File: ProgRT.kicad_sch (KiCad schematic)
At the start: 66 parts

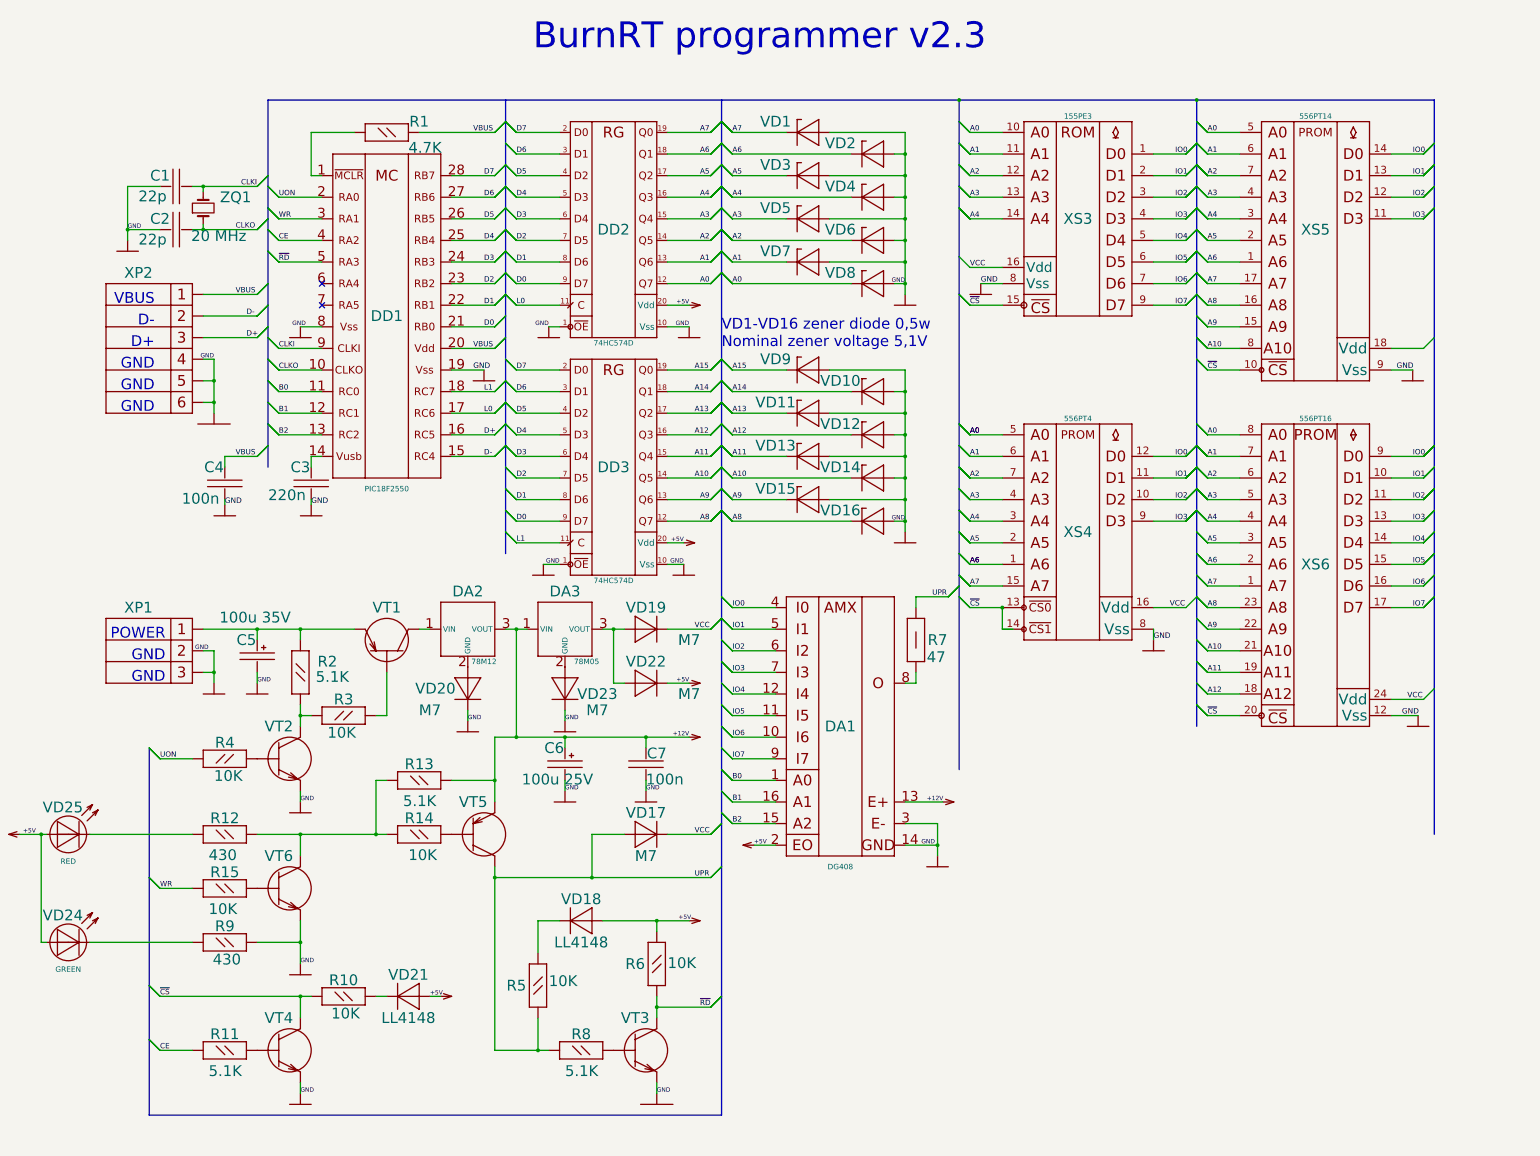
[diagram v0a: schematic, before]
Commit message: PCB from the original single-board layout
Recovered the PCB from schematic and old gerbers. The gerbers didn't contain
recent fixups, these parts need to be placed
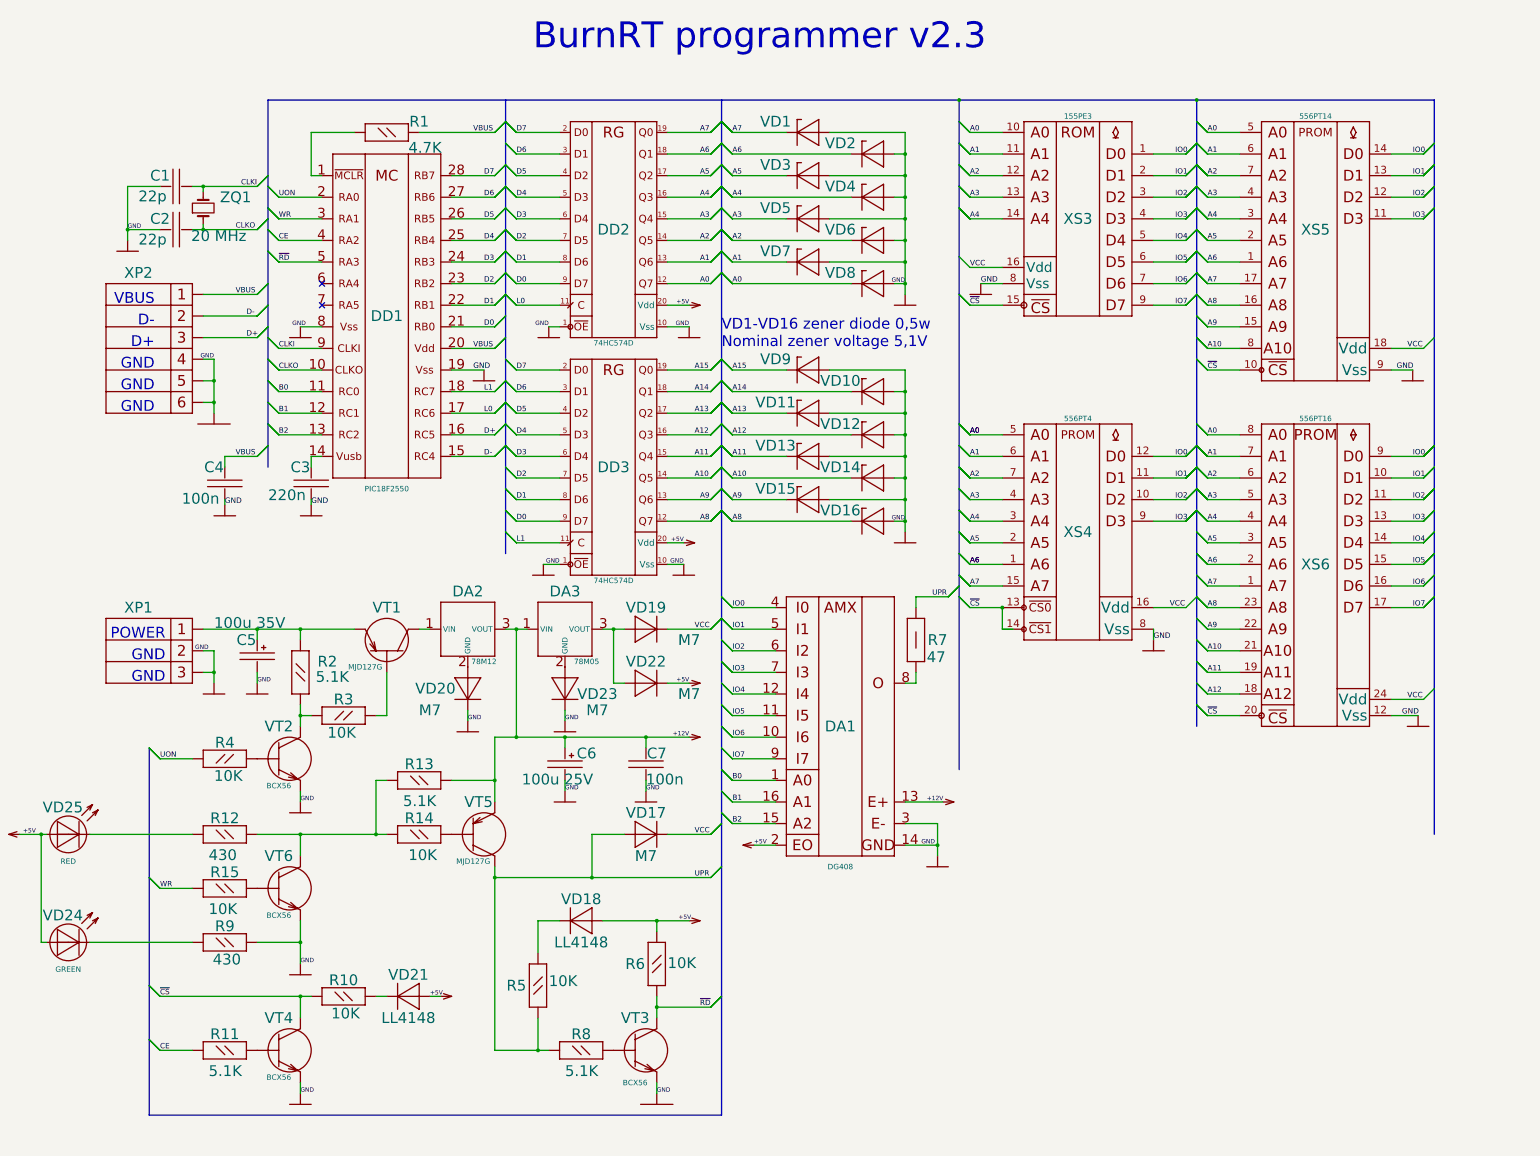
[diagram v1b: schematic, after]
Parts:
- C1, C2: footprint ProgRT: -> Capacitor_SMD:C_0805_2012Metric_Pad1.18x1.45mm_HandSolder
- C3, C4, C7: footprint (none) -> Capacitor_SMD:C_0805_2012Metric_Pad1.18x1.45mm_HandSolder
- C5, C6: footprint (none) -> Capacitor_THT:CP_Radial_D5.0mm_P2.50mm
- VD24, VD25: footprint Socet.SCH.eagle: -> Diode_SMD:D_SOD-123
- VT1, VT5: value КТ973 -> MJD127G; footprint (none) -> Package_TO_SOT_SMD:TO-252-2
- VT2, VT3, VT4, VT6: value КТ503 -> BCX56; footprint (none) -> Package_TO_SOT_SMD:SOT-89-3
- XP2: footprint Connector_USB:USB_Micro-B_Wuerth_629105150521 -> Connector_USB:USB_Mini-B_Lumberg_2486_01_Horizontal
- XS6: footprint Socket:DIP_Socket-24_W4.3_W5.08_W7.62_W10.16_W10.9_3M_224-5248-00-0602J -> Socket:DIP_Socket-24_W11.9_W12.7_W15.24_W17.78_W18.5_3M_224-1275-00-0602J
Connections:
- net +12V: now also C6.1, VT5.3 (E); no longer C6.2 (1), VT5.2 (E)
- net GND: now also C5.2, C6.2; no longer C5.1 (2), C6.1 (2)
- net UPR: now also VT5.2 (C); no longer VT5.1 (C)
- net VCC: now also XS5.18 (Vdd)
- net at R14.2: now also VT5.1 (B); no longer VT5.3 (B)
- net at DA2.1 (VIN): now also VT1.2 (C); no longer VT1.1 (C)
- net at R2.2, XP1.1: now also C5.1, VT1.3 (E); no longer C5.2 (1), VT1.2 (E)
- net at R3.2: now also VT1.1 (B); no longer VT1.3 (B)

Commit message: Add missing parts
ICSP connector and C8 capacitor
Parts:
- added C8: 100n, Capacitor_SMD:C_0805_2012Metric_Pad1.18x1.45mm_HandSolder, symbol ProgRT-eagle-import:K10-17_1
- added XP3: Conn_01x06, Connector_PinHeader_2.54mm:PinHeader_1x06_P2.54mm_Vertical, symbol Connector_Generic:Conn_01x06
- VD24, VD25: footprint Diode_SMD:D_SOD-123 -> Diode_SMD:D_SOD-123F
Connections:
- net +5V: now also C8.2 (1)
- net D5: now also XP3.6 (Pin_6)
- net D6: now also XP3.5 (Pin_5)
- net D7: now also XP3.4 (Pin_4)
- net GND: now also C8.1 (2), XP3.3 (Pin_3)
- net VBUS: now also XP3.2 (Pin_2)
- net MCLR: now reaches DD1.1 (!MCLR), R1.1
- net MCLR: now also XP3.1 (Pin_1)

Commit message: Small footprint corrections
- use SMF footprint for Zener diodes, easier to hand-solder
- use larger footprint for polar caps, extends availability
- use 3216 LEDs, easier available and easier to hand-solder
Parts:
- C5, C6: footprint Capacitor_THT:CP_Radial_D5.0mm_P2.50mm -> Capacitor_THT:CP_Radial_D8.0mm_P3.80mm
- C8: footprint Capacitor_SMD:C_0805_2012Metric_Pad1.18x1.45mm_HandSolder -> Capacitor_SMD:C_1206_3216Metric_Pad1.33x1.80mm_HandSolder
- VD1, VD10, VD11, VD12, VD13, VD14, VD15, VD16, VD2, VD3, VD4, VD5, VD6, VD7, VD8, VD9: footprint Diode_SMD:D_SOD-123 -> Diode_SMD:D_SMF
- VD24, VD25: footprint Diode_SMD:D_SOD-123F -> LED_SMD:LED_1206_3216Metric_Pad1.42x1.75mm_HandSolder
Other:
- note removed: "BurnRT programmer v2.3"
- title: (none) -> BurnRT programmer
- moved on the sheet: C1, C2, C3, C4, C5, C6, C7, C8, DA1, DA2, DA3, DD1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

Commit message: Use MiniMELF Zeners
Change Zener diodes package again to MiniMELF. Should be easier to hand-solder.
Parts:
- VD1, VD10, VD11, VD12, VD13, VD14, VD15, VD16, VD2, VD3, VD4, VD5, VD6, VD7, VD8, VD9: footprint Diode_SMD:D_SMF -> Diode_SMD:D_MiniMELF
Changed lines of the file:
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@@
       (effects (font (size 1.27 1.27)) hide)
     )
-    (property "Footprint" "Diode_SMD:D_SMF" (id 2) (at 220.98 66.04 0)
+    (property "Footprint" "Diode_SMD:D_MiniMELF" (id 2) (at 220.98 66.04 0)
       (effects (font (size 1.27 1.27)) hide)
     )
@@
       (effects (font (size 1.27 1.27)) hide)
     )
-    (property "Footprint" "Diode_SMD:D_SMF" (id 2) (at 236.22 50.8 0)
+    (property "Footprint" "Diode_SMD:D_MiniMELF" (id 2) (at 236.22 50.8 0)
       (effects (font (size 1.27 1.27)) hide)
     )
@@
       (effects (font (size 1.27 1.27)) hide)
     )
-    (property "Footprint" "Diode_SMD:D_SMF" (id 2) (at 236.22 106.68 0)
+    (property "Footprint" "Diode_SMD:D_MiniMELF" (id 2) (at 236.22 106.68 0)
       (effects (font (size 1.27 1.27)) hide)
     )
@@
       (effects (font (size 1.27 1.27)) hide)
     )
-    (property "Footprint" "Diode_SMD:D_SMF" (id 2) (at 236.22 127 0)
+    (property "Footprint" "Diode_SMD:D_MiniMELF" (id 2) (at 236.22 127 0)
       (effects (font (size 1.27 1.27)) hide)
     )
@@
       (effects (font (size 1.27 1.27)) hide)
     )
-    (property "Footprint" "Diode_SMD:D_SMF" (id 2) (at 220.98 76.2 0)
+    (property "Footprint" "Diode_SMD:D_MiniMELF" (id 2) (at 220.98 76.2 0)
       (effects (font (size 1.27 1.27)) hide)
     )
@@
       (effects (font (size 1.27 1.27)) hide)
     )
-    (property "Footprint" "Diode_SMD:D_SMF" (id 2) (at 220.98 121.92 0)
+    (property "Footprint" "Diode_SMD:D_MiniMELF" (id 2) (at 220.98 121.92 0)
       (effects (font (size 1.27 1.27)) hide)
     )
@@
       (effects (font (size 1.27 1.27)) hide)
     )
-    (property "Footprint" "Diode_SMD:D_SMF" (id 2) (at 236.22 116.84 0)
+    (property "Footprint" "Diode_SMD:D_MiniMELF" (id 2) (at 236.22 116.84 0)
       (effects (font (size 1.27 1.27)) hide)
     )
@@
       (effects (font (size 1.27 1.27)) hide)
     )
-    (property "Footprint" "Diode_SMD:D_SMF" (id 2) (at 220.98 55.88 0)
+    (property "Footprint" "Diode_SMD:D_MiniMELF" (id 2) (at 220.98 55.88 0)
       (effects (font (size 1.27 1.27)) hide)
     )
@@
       (effects (font (size 1.27 1.27)) hide)
     )
-    (property "Footprint" "Diode_SMD:D_SMF" (id 2) (at 220.98 132.08 0)
+    (property "Footprint" "Diode_SMD:D_MiniMELF" (id 2) (at 220.98 132.08 0)
       (effects (font (size 1.27 1.27)) hide)
     )
@@
       (effects (font (size 1.27 1.27)) hide)
     )
-    (property "Footprint" "Diode_SMD:D_SMF" (id 2) (at 236.22 71.12 0)
+    (property "Footprint" "Diode_SMD:D_MiniMELF" (id 2) (at 236.22 71.12 0)
       (effects (font (size 1.27 1.27)) hide)
     )
@@
       (effects (font (size 1.27 1.27)) hide)
     )
-    (property "Footprint" "Diode_SMD:D_SMF" (id 2) (at 220.98 45.72 0)
+    (property "Footprint" "Diode_SMD:D_MiniMELF" (id 2) (at 220.98 45.72 0)
       (effects (font (size 1.27 1.27)) hide)
     )
@@
       (effects (font (size 1.27 1.27)) hide)
     )
-    (property "Footprint" "Diode_SMD:D_SMF" (id 2) (at 236.22 137.16 0)
+    (property "Footprint" "Diode_SMD:D_MiniMELF" (id 2) (at 236.22 137.16 0)
       (effects (font (size 1.27 1.27)) hide)
     )
@@
       (effects (font (size 1.27 1.27)) hide)
     )
-    (property "Footprint" "Diode_SMD:D_SMF" (id 2) (at 220.98 101.6 0)
+    (property "Footprint" "Diode_SMD:D_MiniMELF" (id 2) (at 220.98 101.6 0)
       (effects (font (size 1.27 1.27)) hide)
     )
@@
       (effects (font (size 1.27 1.27)) hide)
     )
-    (property "Footprint" "Diode_SMD:D_SMF" (id 2) (at 220.98 111.76 0)
+    (property "Footprint" "Diode_SMD:D_MiniMELF" (id 2) (at 220.98 111.76 0)
       (effects (font (size 1.27 1.27)) hide)
     )
@@
       (effects (font (size 1.27 1.27)) hide)
     )
-    (property "Footprint" "Diode_SMD:D_SMF" (id 2) (at 236.22 81.28 0)
+    (property "Footprint" "Diode_SMD:D_MiniMELF" (id 2) (at 236.22 81.28 0)
       (effects (font (size 1.27 1.27)) hide)
     )
@@
       (effects (font (size 1.27 1.27)) hide)
     )
-    (property "Footprint" "Diode_SMD:D_SMF" (id 2) (at 236.22 60.96 0)
+    (property "Footprint" "Diode_SMD:D_MiniMELF" (id 2) (at 236.22 60.96 0)
       (effects (font (size 1.27 1.27)) hide)
     )
@@
     )
     (path "/92c916b6-8cc9-4956-b8f8-66382389fe45"
-      (reference "VD1") (unit 1) (value "BZV55-C5V1") (footprint "Diode_SMD:D_SMF")
+      (reference "VD1") (unit 1) (value "BZV55-C5V1") (footprint "Diode_SMD:D_MiniMELF")
     )
     (path "/20ab95ab-18f4-45b8-bd52-a946b3051a28"
-      (reference "VD2") (unit 1) (value "BZV55-C5V1") (footprint "Diode_SMD:D_SMF")
+      (reference "VD2") (unit 1) (value "BZV55-C5V1") (footprint "Diode_SMD:D_MiniMELF")
     )
     (path "/66f2f1b9-2566-4dc2-a4aa-07fcb617484b"
-      (reference "VD3") (unit 1) (value "BZV55-C5V1") (footprint "Diode_SMD:D_SMF")
+      (reference "VD3") (unit 1) (value "BZV55-C5V1") (footprint "Diode_SMD:D_MiniMELF")
     )
     (path "/e2ec694e-33a6-4b44-8fef-1919488dec0a"
-      (reference "VD4") (unit 1) (value "BZV55-C5V1") (footprint "Diode_SMD:D_SMF")
+      (reference "VD4") (unit 1) (value "BZV55-C5V1") (footprint "Diode_SMD:D_MiniMELF")
     )
     (path "/06dee028-9e33-4ad8-88ea-367767477e3c"
-      (reference "VD5") (unit 1) (value "BZV55-C5V1") (footprint "Diode_SMD:D_SMF")
+      (reference "VD5") (unit 1) (value "BZV55-C5V1") (footprint "Diode_SMD:D_MiniMELF")
     )
     (path "/75cf632d-3942-41dd-97f1-f7ad380f9840"
-      (reference "VD6") (unit 1) (value "BZV55-C5V1") (footprint "Diode_SMD:D_SMF")
+      (reference "VD6") (unit 1) (value "BZV55-C5V1") (footprint "Diode_SMD:D_MiniMELF")
     )
     (path "/3f3355da-5a3a-4cb9-98d8-2b3c11a7a282"
-      (reference "VD7") (unit 1) (value "BZV55-C5V1") (footprint "Diode_SMD:D_SMF")
+      (reference "VD7") (unit 1) (value "BZV55-C5V1") (footprint "Diode_SMD:D_MiniMELF")
     )
     (path "/dc107f3b-26ba-4b3c-9648-1822b2a8f9c7"
-      (reference "VD8") (unit 1) (value "BZV55-C5V1") (footprint "Diode_SMD:D_SMF")
+      (reference "VD8") (unit 1) (value "BZV55-C5V1") (footprint "Diode_SMD:D_MiniMELF")
     )
     (path "/c558d337-f7df-449b-9c19-e58304db43b0"
-      (reference "VD9") (unit 1) (value "BZV55-C5V1") (footprint "Diode_SMD:D_SMF")
+      (reference "VD9") (unit 1) (value "BZV55-C5V1") (footprint "Diode_SMD:D_MiniMELF")
     )
     (path "/38f98618-bfbe-4efa-b338-103b7c00ea44"
-      (reference "VD10") (unit 1) (value "BZV55-C5V1") (footprint "Diode_SMD:D_SMF")
+      (reference "VD10") (unit 1) (value "BZV55-C5V1") (footprint "Diode_SMD:D_MiniMELF")
     )
     (path "/db270bbc-71ee-4577-9858-f067bdb562bc"
-      (reference "VD11") (unit 1) (value "BZV55-C5V1") (footprint "Diode_SMD:D_SMF")
+      (reference "VD11") (unit 1) (value "BZV55-C5V1") (footprint "Diode_SMD:D_MiniMELF")
     )
     (path "/5edc08d5-c74a-4763-be15-68ab206e18a7"
-      (reference "VD12") (unit 1) (value "BZV55-C5V1") (footprint "Diode_SMD:D_SMF")
+      (reference "VD12") (unit 1) (value "BZV55-C5V1") (footprint "Diode_SMD:D_MiniMELF")
     )
     (path "/534699c0-c88e-4875-aae0-4dd2f1a74dc0"
-      (reference "VD13") (unit 1) (value "BZV55-C5V1") (footprint "Diode_SMD:D_SMF")
+      (reference "VD13") (unit 1) (value "BZV55-C5V1") (footprint "Diode_SMD:D_MiniMELF")
     )
     (path "/3d45ba9c-6fa5-4044-9227-ffbfc6ea50a5"
-      (reference "VD14") (unit 1) (value "BZV55-C5V1") (footprint "Diode_SMD:D_SMF")
+      (reference "VD14") (unit 1) (value "BZV55-C5V1") (footprint "Diode_SMD:D_MiniMELF")
     )
     (path "/6ea42f30-4e8d-4083-bf73-1fcb3290f040"
-      (reference "VD15") (unit 1) (value "BZV55-C5V1") (footprint "Diode_SMD:D_SMF")
+      (reference "VD15") (unit 1) (value "BZV55-C5V1") (footprint "Diode_SMD:D_MiniMELF")
     )
     (path "/b818c93d-49a5-4c46-97cc-bd618f6f38c4"
-      (reference "VD16") (unit 1) (value "BZV55-C5V1") (footprint "Diode_SMD:D_SMF")
+      (reference "VD16") (unit 1) (value "BZV55-C5V1") (footprint "Diode_SMD:D_MiniMELF")
     )
     (path "/3bd1362f-f632-4761-ac21-da011354d1f0"
